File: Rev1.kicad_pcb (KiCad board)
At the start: 2 copper layers, 152.8 x 71.5 mm, 105 parts, among them J1 Conn_01x08_Socket, J10 Conn_01x08_Socket, J11 Power, J12 Conn_01x08_Socket, J13 Conn_01x08_Socket, J2 Conn_01x08_Socket, J3 Conn_01x08_Socket, J4 Conn_01x08_Socket, J5 Conn_01x08_Socket, J6 Conn_01x08_Socket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

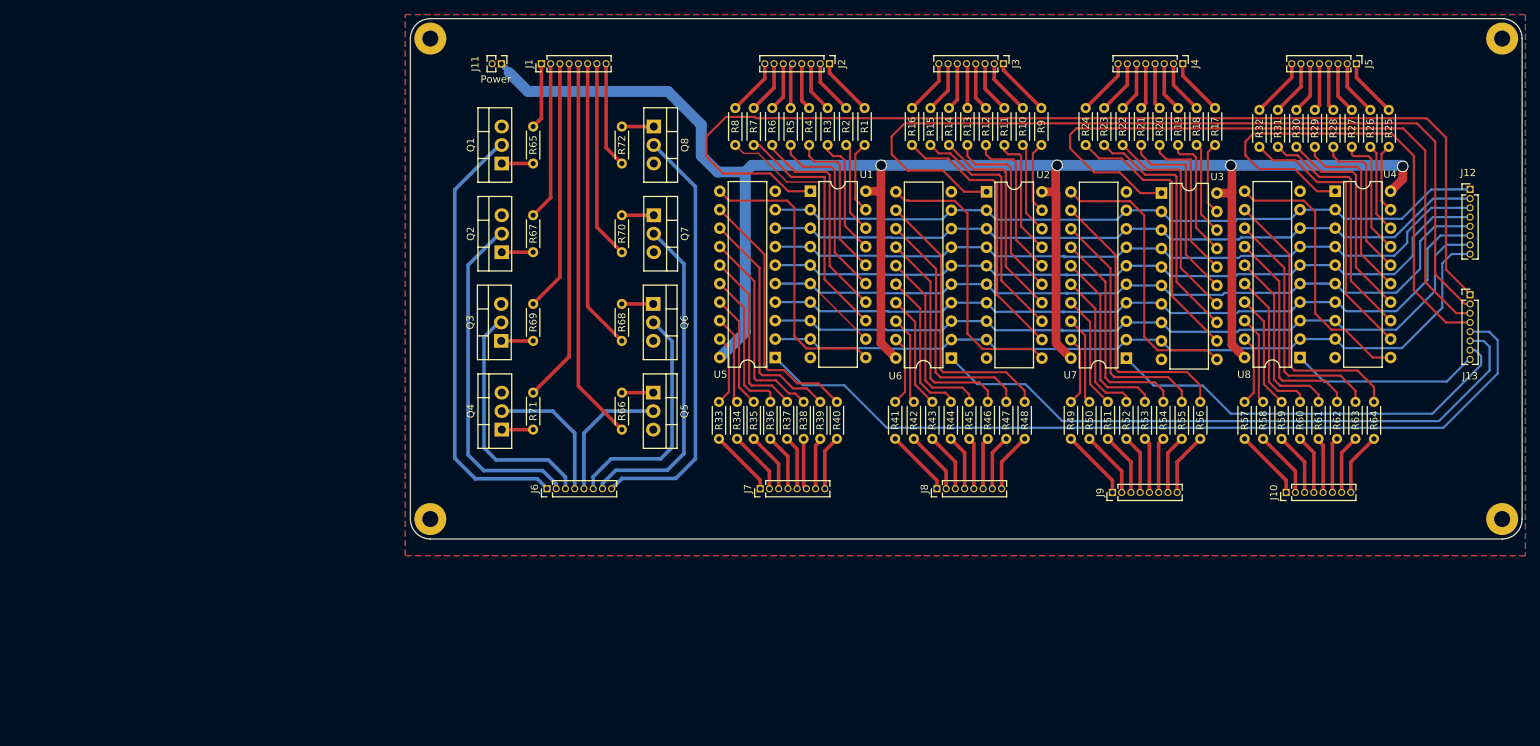
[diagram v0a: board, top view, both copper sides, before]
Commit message: Added decoupling caps. Rerouted
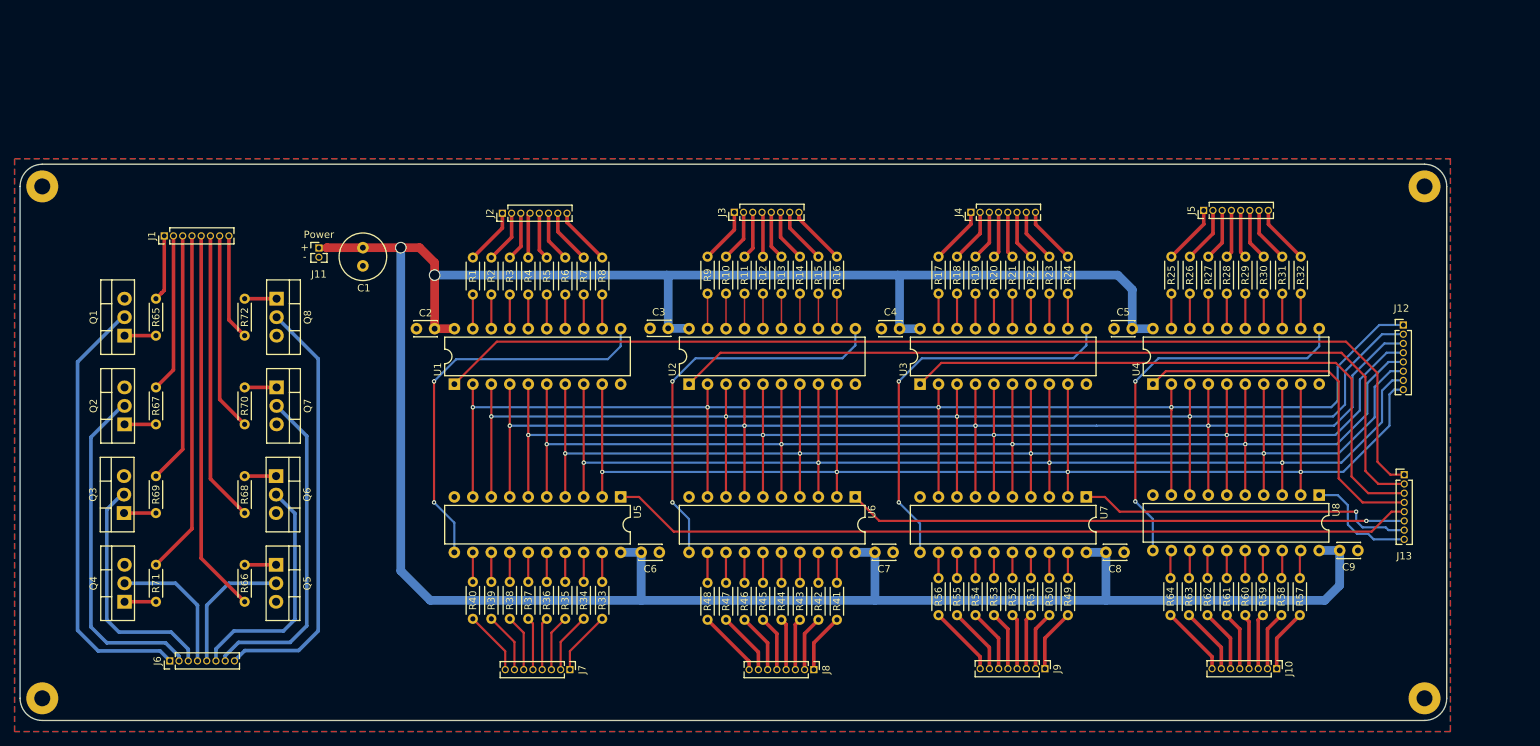
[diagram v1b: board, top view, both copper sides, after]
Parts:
- added C1: Bulk, Capacitor_THT:C_Radial_D6.3mm_H7.0mm_P2.50mm, F.Cu at (97.4, 54.1)
- added C2: Dcp, Capacitor_THT:C_Disc_D3.0mm_W2.0mm_P2.50mm, F.Cu at (107.3, 65.3)
- added C3: Dcp, Capacitor_THT:C_Disc_D3.0mm_W2.0mm_P2.50mm, F.Cu at (139.4, 65.2)
- added C4: Dcp, Capacitor_THT:C_Disc_D3.0mm_W2.0mm_P2.50mm, F.Cu at (171.2, 65.3)
- added C5: Dcp, Capacitor_THT:C_Disc_D3.0mm_W2.0mm_P2.50mm, F.Cu at (203.2, 65.3)
- added C6: Dcp, Capacitor_THT:C_Disc_D3.0mm_W2.0mm_P2.50mm, F.Cu at (135.7, 96.0)
- added C7: Dcp, Capacitor_THT:C_Disc_D3.0mm_W2.0mm_P2.50mm, F.Cu at (167.8, 96.0)
- added C8: Dcp, Capacitor_THT:C_Disc_D3.0mm_W2.0mm_P2.50mm, F.Cu at (199.5, 96.0)
- added C9: Dcp, Capacitor_THT:C_Disc_D3.0mm_W2.0mm_P2.50mm, F.Cu at (231.7, 95.8)
- moved H4 58.8 mm to (53.3, 116.1)
- moved R1 57.6 mm to (112.5, 55.5)
- moved H1 57.1 mm to (53.3, 45.7)
- moved Q6 57.0 mm to (85.5, 85.5)
- moved Q7 57.0 mm to (85.5, 73.3)
- moved Q8 57.0 mm to (85.5, 61.2)
- moved J1 57.0 mm to (70.1, 52.5)
- moved J6 57.0 mm to (70.9, 110.9)
- moved Q1 57.0 mm to (64.6, 66.2)
- moved Q2 57.0 mm to (64.6, 78.4)
- moved Q3 57.0 mm to (64.6, 90.6)
- moved Q4 57.0 mm to (64.6, 102.8)
- moved Q5 57.0 mm to (85.5, 97.7)
- moved R65 57.0 mm to (69.0, 66.2)
- moved R66 57.0 mm to (81.2, 97.7)
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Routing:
- net VCC: track 252.2 -> 365.7 mm, vias 4 -> 2
- net /D0: track 101.2 -> 197.1 mm, vias 0 -> 4
- net /D1: track 101.6 -> 194.5 mm, vias 0 -> 4
- net /D2: track 103.0 -> 191.8 mm, vias 0 -> 4
- net /D3: track 104.1 -> 189.2 mm, vias 0 -> 4
- net /D4: track 105.5 -> 186.6 mm, vias 0 -> 4
- net /D5: track 106.2 -> 184.1 mm, vias 0 -> 4
- net /D6: track 107.1 -> 181.6 mm, vias 0 -> 4
- net /D7: track 108.3 -> 179.1 mm, vias 0 -> 4
- net Net-(U7-Q7): track 39.2 -> 3.55 mm
- net Net-(U8-Q7): track 38.8 -> 3.85 mm
- net Net-(U6-Q7): track 38.8 -> 4.18 mm
- net Net-(U3-Q7): track 38.3 -> 4.83 mm
- net Net-(U4-Q7): track 38.0 -> 4.82 mm
- net Net-(U1-Q7): track 37.8 -> 4.70 mm
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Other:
- board size 152.8 x 71.5 mm -> 196.1 x 76.5 mm
- board text added: "+"
- board text added: "-"
